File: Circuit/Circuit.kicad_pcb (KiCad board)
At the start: 2 copper layers, 113 x 52.1 mm, 22 parts, among them J1 UE27AC54100, J2 22-23-2021, J3 22-23-2021, J4 22-23-2021, Q1 AO3401A, Q2 2N2222A, U1 L4978

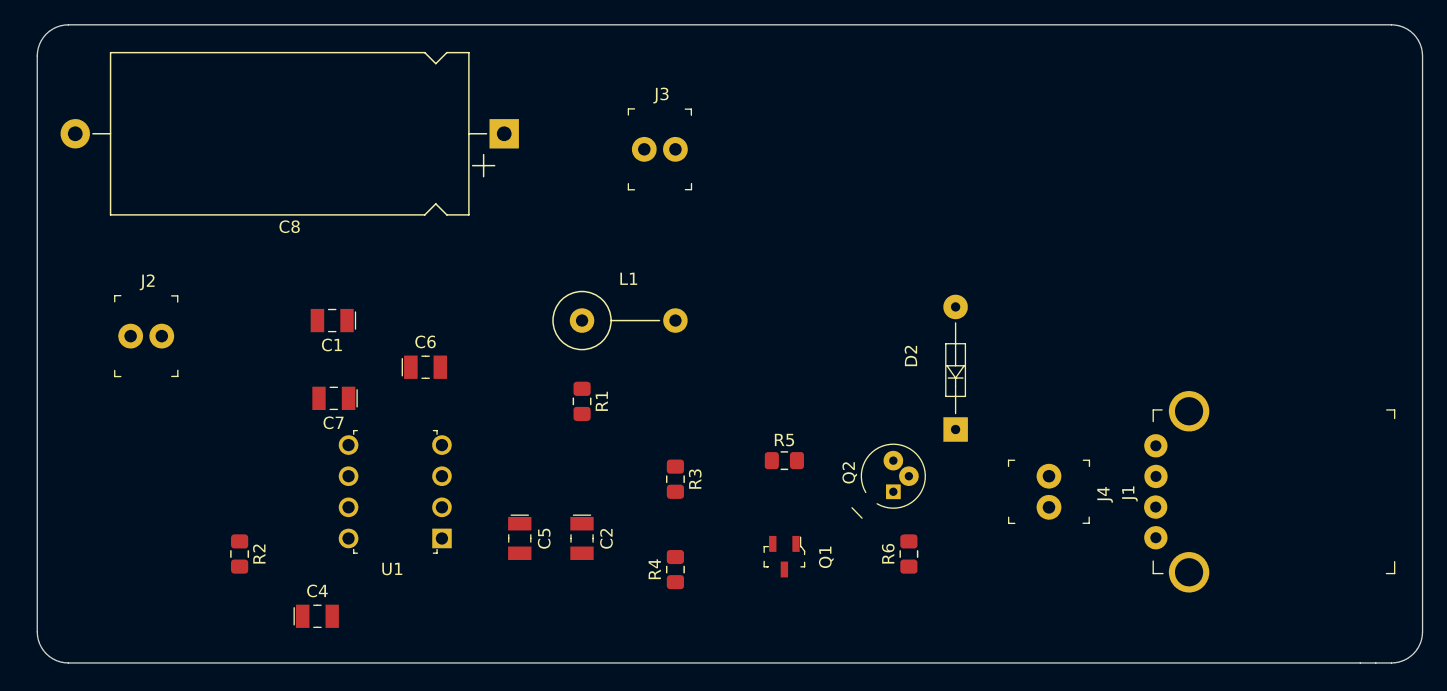
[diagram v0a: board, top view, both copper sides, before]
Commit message: Soon finnished with PCB
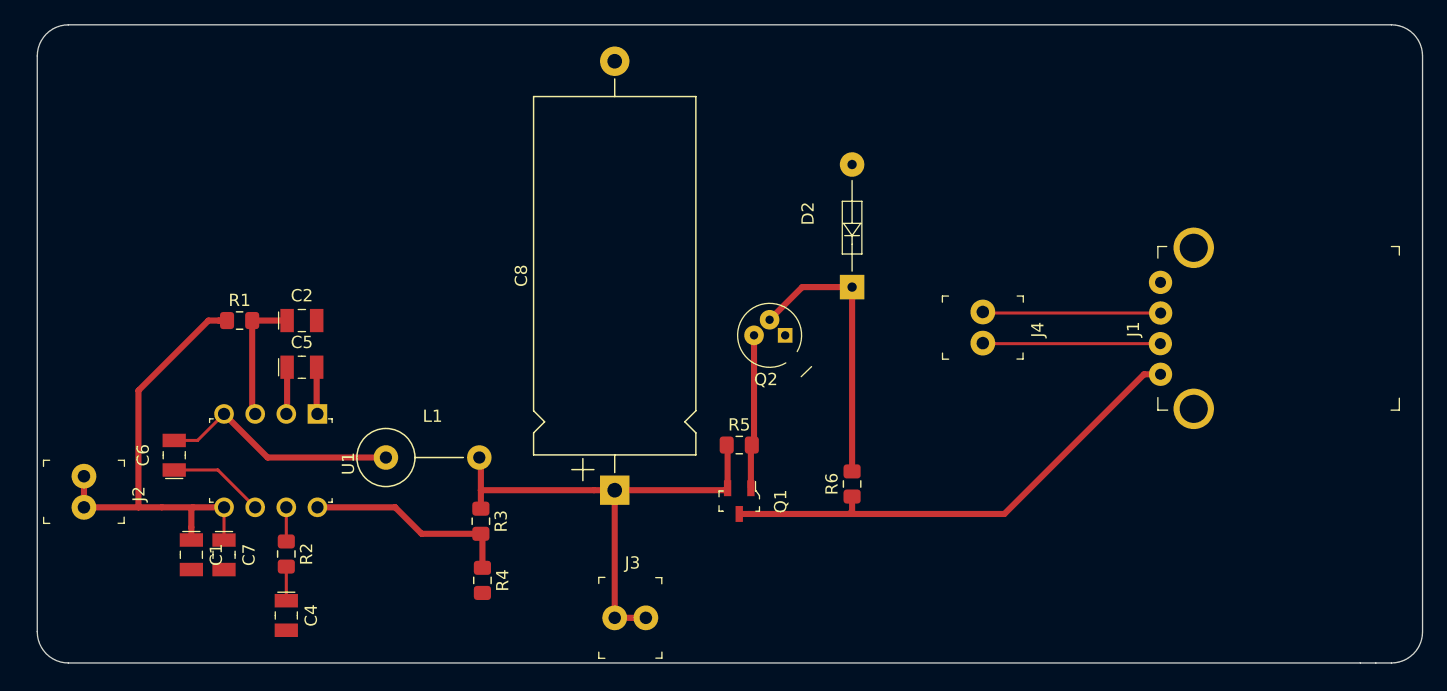
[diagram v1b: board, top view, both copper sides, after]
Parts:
- moved J3 38.3 mm to (122.0, 117.0)
- moved C8 30.4 mm to (122.0, 106.6), turned to 90 degrees
- moved C2 29.0 mm to (96.5, 92.7), turned to 0 degrees
- moved R1 28.7 mm to (91.4, 92.7), turned to 0 degrees
- moved C5 22.6 mm to (96.5, 96.5), turned to 0 degrees
- moved C1 22.3 mm to (87.5, 111.8), turned to 270 degrees
- moved C6 21.7 mm to (86.1, 103.7), turned to 90 degrees
- moved L1 19.5 mm to (103.4, 103.9)
- moved R3 16.2 mm to (111.1, 109.1)
- moved R4 15.8 mm to (111.3, 113.9), turned to 270 degrees
- moved C7 15.6 mm to (90.2, 111.8), turned to 270 degrees
- moved Q2 15.5 mm to (136.0, 93.9), turned to 180 degrees
- moved J4 14.4 mm to (152.1, 92.0)
- moved U1 14.4 mm to (97.8, 100.3), turned to 270 degrees
- moved D2 14.4 mm to (141.4, 90.0)
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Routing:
- net +5V: track 0.00 -> 40.9 mm
- net Net-(J1-Pad1): track 0.00 -> 40.6 mm
- net +12V: track 0.00 -> 38.5 mm
- net Net-(D2-Pad1): track 0.00 -> 22.9 mm
- net Net-(C6-Pad2): track 0.00 -> 19.6 mm
- net Net-(R3-Pad2): track 0.00 -> 17.1 mm
- net /D+: track 0.00 -> 14.5 mm
- net /D-: track 0.00 -> 14.5 mm
- net Net-(Q1-Pad1): track 0.00 -> 12.6 mm
- net Net-(C2-Pad1): track 0.00 -> 10.6 mm
- net Net-(C6-Pad1): track 0.00 -> 7.87 mm
- net GND: track 0.00 -> 3.93 mm
- net Net-(C5-Pad1): track 0.00 -> 3.93 mm
- net Net-(R2-Pad1): track 0.00 -> 2.78 mm
- net Net-(C4-Pad1): track 0.00 -> 2.78 mm

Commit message: Finnished PCB
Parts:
- added J5: 22-23-2021, digikey-footprints:PinHeader_1x2_P2.54mm_Drill1.02mm, F.Cu at (151.3, 117.2)
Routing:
- net GND: track 3.93 -> 36.7 mm, vias 0 -> 5
- net Net-(J1-Pad1): track 40.6 -> 51.8 mm
- added copper zone on B.Cu, net GND
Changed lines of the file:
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@@
     (thickness 1.6)
     (drawings 10)
-    (tracks 65)
+    (tracks 85)
     (zones 0)
-    (modules 22)
+    (modules 23)
     (nets 17)
   )
@@
   (layers
     (0 F.Cu signal)
-    (31 B.Cu signal)
+    (31 B.Cu signal hide)
     (32 B.Adhes user)
     (33 F.Adhes user)
@@
   )
   (setup
-    (last_trace_width 0.25)
+    (last_trace_width 0.5)
     (user_trace_width 0.5)
     (trace_clearance 0.2)
     (zone_clearance 0.508)
-    (zone_45_only no)
+    (zone_45_only yes)
     (trace_min 0.2)
     (via_size 0.8)
@@
     (solder_mask_min_width 0.25)
     (aux_axis_origin 0 0)
-    (visible_elements FFFDFF7F)
+    (visible_elements FFFDF77F)
     (pcbplotparams
       (layerselection 0x010fc_ffffffff)
@@
     (add_net "Net-(R3-Pad2)")
   )
+  (module digikey-footprints:PinHeader_1x2_P2.54mm_Drill1.02mm (layer F.Cu)
+    (at 151.257 117.1575)
+    (descr http://www.molex.com/pdm_docs/sd/022232031_sd.pdf)
+    (fp_text reference J5 (at 1.45 -4.48) (layer F.SilkS)
+      (effects (font (size 1 1) (thickness 0.15)))
+    )
+    (fp_text value 22-23-2021 (at 1.23 4.72) (layer F.Fab)
+      (effects (font (size 1 1) (thickness 0.15)))
+    )
+    (fp_line (start -1.2 -3.17) (end 3.73 -3.17) (layer F.Fab) (width 0.1))
+    (fp_line (start -1.2 -3.17) (end -1.2 3.17) (layer F.Fab) (width 0.1))
+    (fp_line (start 3.73 -3.17) (end 3.73 3.17) (layer F.Fab) (width 0.1))
+    (fp_line (start -1.2 3.17) (end 3.73 3.17) (layer F.Fab) (width 0.1))
+    (fp_line (start 3.85 3.29) (end 3.35 3.29) (layer F.SilkS) (width 0.1))
+    (fp_line (start 3.85 3.29) (end 3.85 2.79) (layer F.SilkS) (width 0.1))
+    (fp_line (start -1.3 3.3) (end -0.8 3.3) (layer F.SilkS) (width 0.1))
+    (fp_line (start -1.3 3.3) (end -1.3 2.8) (layer F.SilkS) (width 0.1))
+    (fp_line (start -1.3 -3.3) (end -0.8 -3.3) (layer F.SilkS) (width 0.1))
+    (fp_line (start -1.3 -3.3) (end -1.3 -2.8) (layer F.SilkS) (width 0.1))
+    (fp_line (start 3.84 -3.28) (end 3.34 -3.28) (layer F.SilkS) (width 0.1))
+    (fp_line (start 3.84 -3.28) (end 3.84 -2.78) (layer F.SilkS) (width 0.1))
+    (fp_line (start 3.98 -3.42) (end -1.45 -3.42) (layer F.CrtYd) (width 0.05))
+    (fp_line (start 3.98 -3.42) (end 3.98 3.42) (layer F.CrtYd) (width 0.05))
+    (fp_line (start -1.45 -3.42) (end -1.45 3.42) (layer F.CrtYd) (width 0.05))
+    (fp_line (start 3.98 3.42) (end -1.45 3.42) (layer F.CrtYd) (width 0.05))
+    (fp_text user %R (at 1.25 0.03) (layer F.Fab)
+      (effects (font (size 1 1) (thickness 0.15)))
+    )
+    (pad 2 thru_hole circle (at 2.54 0) (size 2.02 2.02) (drill 1.02) (layers *.Cu *.Mask)
+      (net 9 "Net-(J1-Pad1)"))
+    (pad 1 thru_hole circle (at 0 0) (size 2.02 2.02) (drill 1.02) (layers *.Cu *.Mask)
+      (net 9 "Net-(J1-Pad1)"))
+  )
   (module Capacitor_THT:CP_Axial_L29.0mm_D13.0mm_P35.00mm_Horizontal (layer F.Cu)
     (at 122.047 106.553 90)
@@
   (segment (start 97.725 100.265) (end 97.79 100.33) (width 0.5) (layer F.Cu) (net 1))
   (segment (start 97.725 96.52) (end 97.725 100.265) (width 0.5) (layer F.Cu) (net 1))
+  (via (at 102.108 92.71) (size 0.8) (drill 0.4) (layers F.Cu B.Cu) (net 1))
+  (segment (start 97.725 92.71) (end 102.108 92.71) (width 0.5) (layer F.Cu) (net 1))
+  (via (at 102.108 96.52) (size 0.8) (drill 0.4) (layers F.Cu B.Cu) (net 1))
+  (segment (start 97.725 96.52) (end 102.108 96.52) (width 0.5) (layer F.Cu) (net 1))
+  (segment (start 90.17 117.856) (end 90.294 117.98) (width 0.5) (layer F.Cu) (net 1))
+  (segment (start 93.8 117.98) (end 95.25 117.98) (width 0.5) (layer F.Cu) (net 1))
+  (segment (start 90.294 117.98) (end 93.8 117.98) (width 0.5) (layer F.Cu) (net 1))
+  (segment (start 90.17 113.03) (end 90.17 117.856) (width 0.5) (layer F.Cu) (net 1))
+  (segment (start 90.167 113.027) (end 90.17 113.03) (width 0.5) (layer F.Cu) (net 1))
+  (segment (start 87.503 113.027) (end 90.167 113.027) (width 0.5) (layer F.Cu) (net 1))
+  (segment (start 90.17 117.856) (end 86.614 117.856) (width 0.5) (layer F.Cu) (net 1))
+  (via (at 86.614 117.856) (size 0.8) (drill 0.4) (layers F.Cu B.Cu) (net 1))
+  (via (at 100.076 118.11) (size 0.8) (drill 0.4) (layers F.Cu B.Cu) (net 1))
+  (segment (start 95.25 117.98) (end 99.946 117.98) (width 0.5) (layer F.Cu) (net 1))
+  (segment (start 99.946 117.98) (end 100.076 118.11) (width 0.5) (layer F.Cu) (net 1))
+  (via (at 111.252 117.856) (size 0.8) (drill 0.4) (layers F.Cu B.Cu) (net 1))
+  (segment (start 111.252 114.935) (end 111.252 117.856) (width 0.5) (layer F.Cu) (net 1))
   (segment (start 90.17 107.95) (end 90.17 110.62) (width 0.25) (layer F.Cu) (net 2))
   (segment (start 78.74 105.41) (end 78.74 107.95) (width 0.5) (layer F.Cu) (net 2))
@@
   (segment (start 153.840498 108.492) (end 141.1945 108.492) (width 0.5) (layer F.Cu) (net 9))
   (segment (start 141.1945 108.492) (end 133.007 108.492) (width 0.5) (layer F.Cu) (net 9))
+  (segment (start 153.797 108.535498) (end 153.840498 108.492) (width 0.5) (layer F.Cu) (net 9))
+  (segment (start 153.797 117.1575) (end 153.797 108.535498) (width 0.5) (layer F.Cu) (net 9))
+  (segment (start 151.257 117.1575) (end 153.797 117.1575) (width 0.5) (layer F.Cu) (net 9))
   (segment (start 152.126 94.595) (end 152.0825 94.5515) (width 0.25) (layer F.Cu) (net 10))
   (segment (start 166.566 94.595) (end 152.126 94.595) (width 0.25) (layer F.Cu) (net 10))
@@
   (segment (start 111.252 110.236) (end 111.125 110.109) (width 0.5) (layer F.Cu) (net 16))
   (segment (start 111.252 112.885) (end 111.252 110.236) (width 0.5) (layer F.Cu) (net 16))
+  (zone (net 1) (net_name GND) (layer B.Cu) (hatch edge 0.508)
+    (connect_pads (clearance 0.508))
+    (min_thickness 0.254)
+    (fill yes (arc_segments 32) (thermal_gap 0.508) (thermal_bridge_width 0.508))
+    (polygon
+      (pts
+        (xy 76.454 70.104) (xy 76.454 119.126) (xy 185.674 119.126) (xy 185.674 70.104)
+      )
+    )
+  )
 )

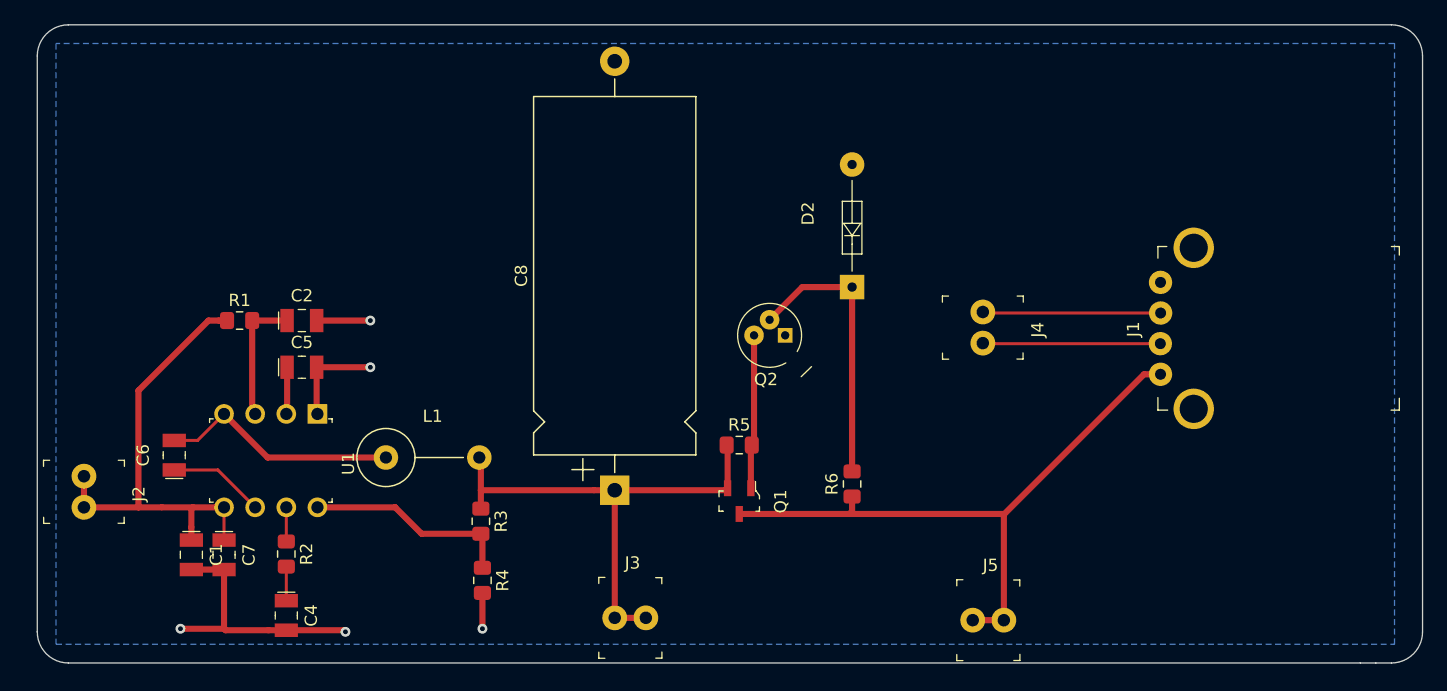
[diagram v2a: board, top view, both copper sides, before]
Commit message: Added 3D models
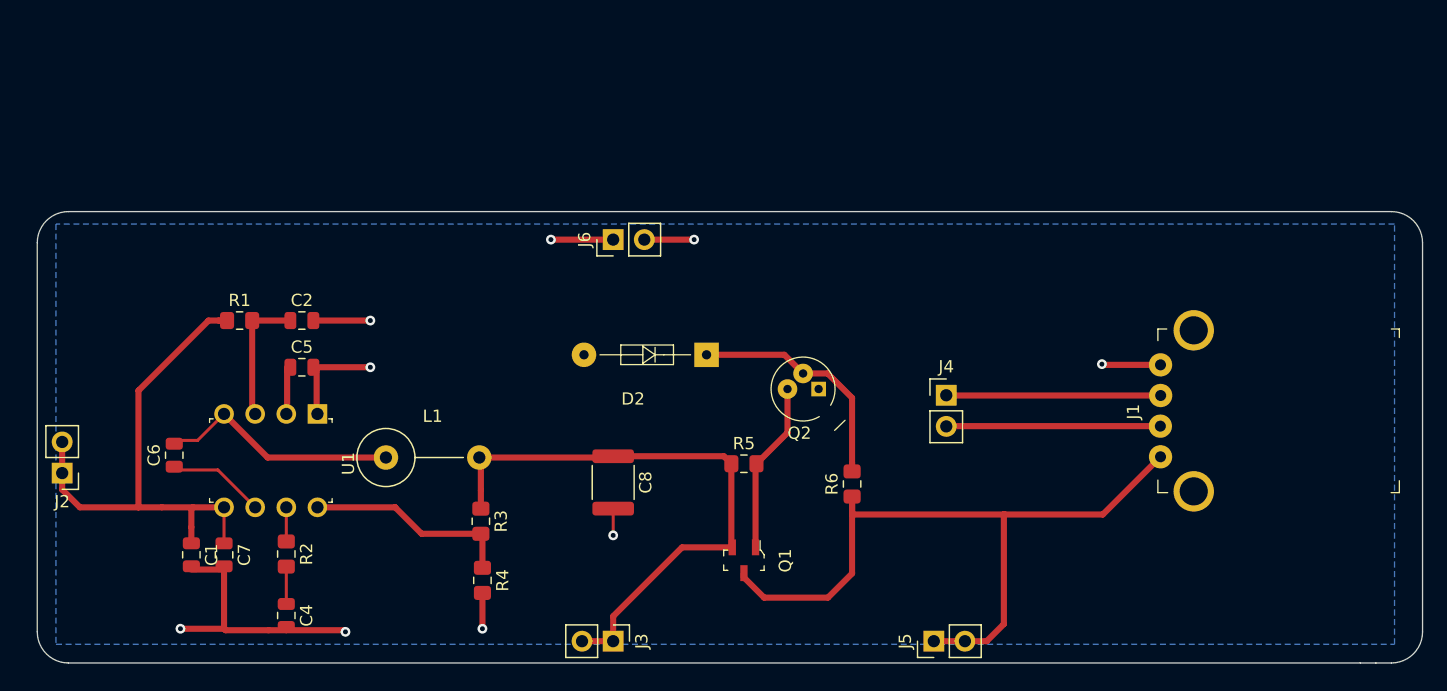
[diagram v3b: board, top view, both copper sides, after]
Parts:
- added J6: 22-23-2021, Connector_PinHeader_2.54mm:PinHeader_1x02_P2.54mm_Vertical, F.Cu at (121.9, 86.1)
- C1, C2, C4, C5, C6, C7: footprint digikey-footprints:SMD-2_3.2x1.5mm -> Capacitor_SMD:C_0805_2012Metric
- C8: footprint Capacitor_THT:CP_Axial_L29.0mm_D13.0mm_P35.00mm_Horizontal -> Capacitor_SMD:C_1812_4532Metric
- J2, J3, J4, J5: footprint digikey-footprints:PinHeader_1x2_P2.54mm_Drill1.02mm -> Connector_PinHeader_2.54mm:PinHeader_1x02_P2.54mm_Vertical
- moved D2 13.1 mm to (129.5, 95.5), turned to 180 degrees
- moved J4 7.42 mm to (149.1, 98.8), turned to 0 degrees
- moved J1 6.73 mm to (169.3, 100.1)
- moved Q2 5.16 mm to (138.7, 98.3)
- moved Q1 4.84 mm to (132.6, 112.3)
- moved J5 3.61 mm to (148.1, 118.9), turned to 90 degrees
- moved J3 1.91 mm to (121.9, 118.9), turned to 270 degrees
- moved J2 1.80 mm to (77.0, 105.2), turned to 180 degrees
- moved R5 1.57 mm to (132.6, 104.4)
- moved C8 0.65 mm to (121.9, 105.9), turned to 270 degrees
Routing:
- net GND: track 36.7 -> 52.8 mm, vias 5 -> 9
- net Net-(J1-Pad1): track 51.8 -> 60.6 mm
- net +5V: track 40.9 -> 48.6 mm
- net +12V: track 38.5 -> 42.2 mm
- net Net-(D2-Pad1): track 22.9 -> 19.3 mm
- net /D-: track 14.5 -> 17.5 mm
- net /D+: track 14.5 -> 17.5 mm
- net Net-(Q1-Pad1): track 12.6 -> 14.0 mm
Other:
- board size 113 x 52.1 mm -> 113 x 36.8 mm

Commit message: Finnished pcb design, and order PCB
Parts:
- added F1: Polyfuse, Fuse:Fuse_Bourns_MF-RHT300, F.Cu at (77.5, 104.1)
- added J7: 22-23-2021, Connector_PinHeader_2.54mm:PinHeader_1x02_P2.54mm_Vertical, F.Cu at (87.1, 86.6)
- added Mnt1: MountingHole_3.5mm, MountingHole:MountingHole_3.5mm, F.Cu at (79.0, 89.2)
- added Mnt2: MountingHole_3.5mm, MountingHole:MountingHole_3.5mm, F.Cu at (79.0, 115.8)
- added Mnt3: MountingHole_3.5mm, MountingHole:MountingHole_3.5mm, F.Cu at (181.9, 89.2)
- added Mnt4: MountingHole_3.5mm, MountingHole:MountingHole_3.5mm, F.Cu at (181.9, 115.8)
- J1: moved to B.Cu
- moved J4 10.5 mm to (158.2, 103.9), turned to 180 degrees
- moved J2 8.38 mm to (77.0, 96.8), turned to 0 degrees
- moved J1 2.62 mm to (169.9, 102.6), turned to 270 degrees
- moved J3 1.05 mm to (120.9, 119.1)
- moved J6 1.05 mm to (120.9, 86.4)
- moved L1 1.05 mm to (102.4, 104.1)
- moved U1 1.05 mm to (96.8, 100.6)
- moved C1 1.05 mm to (86.5, 112.1)
- moved C4 1.05 mm to (94.2, 117.0)
- moved C7 1.05 mm to (89.2, 112.1)
- moved C8 1.05 mm to (120.9, 106.2)
- moved R2 1.05 mm to (94.2, 112.0)
- moved R3 1.05 mm to (110.1, 109.3)
- moved C2 1.05 mm to (95.5, 93.0)
- moved C5 1.05 mm to (95.5, 96.8)
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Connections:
- C1 pad 1: +12V -> Net-(C1-Pad1)
- C7 pad 1: +12V -> Net-(C1-Pad1)
- R1 pad 1: +12V -> Net-(C1-Pad1)
- U1 pad 5: +12V -> Net-(C1-Pad1)
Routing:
- net Net-(C1-Pad1): track 0.00 -> 47.2 mm
- net +12V: track 42.2 -> 7.58 mm
- net /D-: track 17.5 -> 8.97 mm
- net /D+: track 17.5 -> 8.99 mm
- net Net-(J1-Pad1): track 60.6 -> 68.9 mm
- net Net-(C2-Pad1): track 10.6 -> 3.20 mm
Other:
- rule trace_min: 0.2 -> 0.127
- rule via_min_drill: 0.3 -> 0.2
- rule via_min_size: 0.4 -> 0.6
- board text added: "12V"
- board text added: "12V after fuse"
- board text added: "12V to 5V charger"
- board text added: "5V"
- board text added: "D+"
- board text added: "D-"
- board text added: "GND"
- board text added: "Matias GG Design"
